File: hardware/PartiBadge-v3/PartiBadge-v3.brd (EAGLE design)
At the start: 118.9 x 117.7 mm, 26 parts, among them J1 I2C, J2 Supply, T1 MMBT4401-7-F

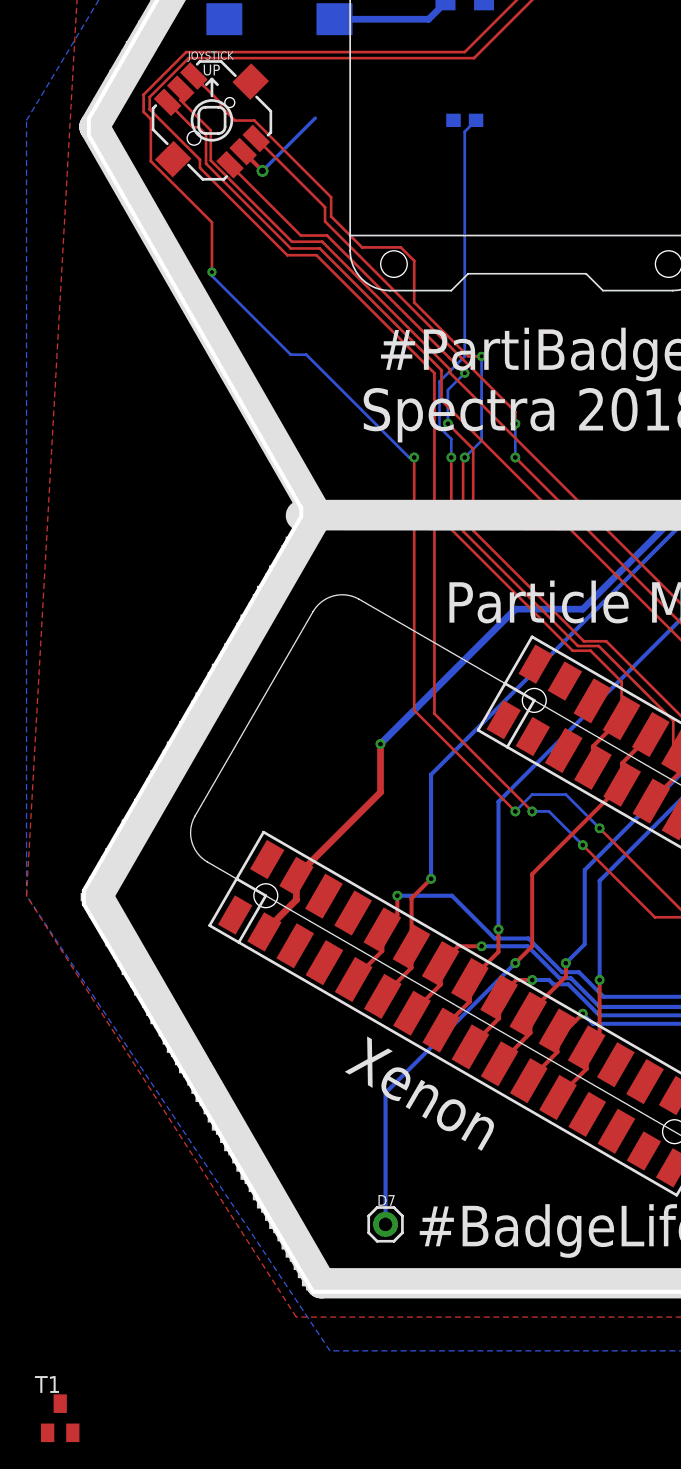
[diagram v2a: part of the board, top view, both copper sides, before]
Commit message: added transistor to layout
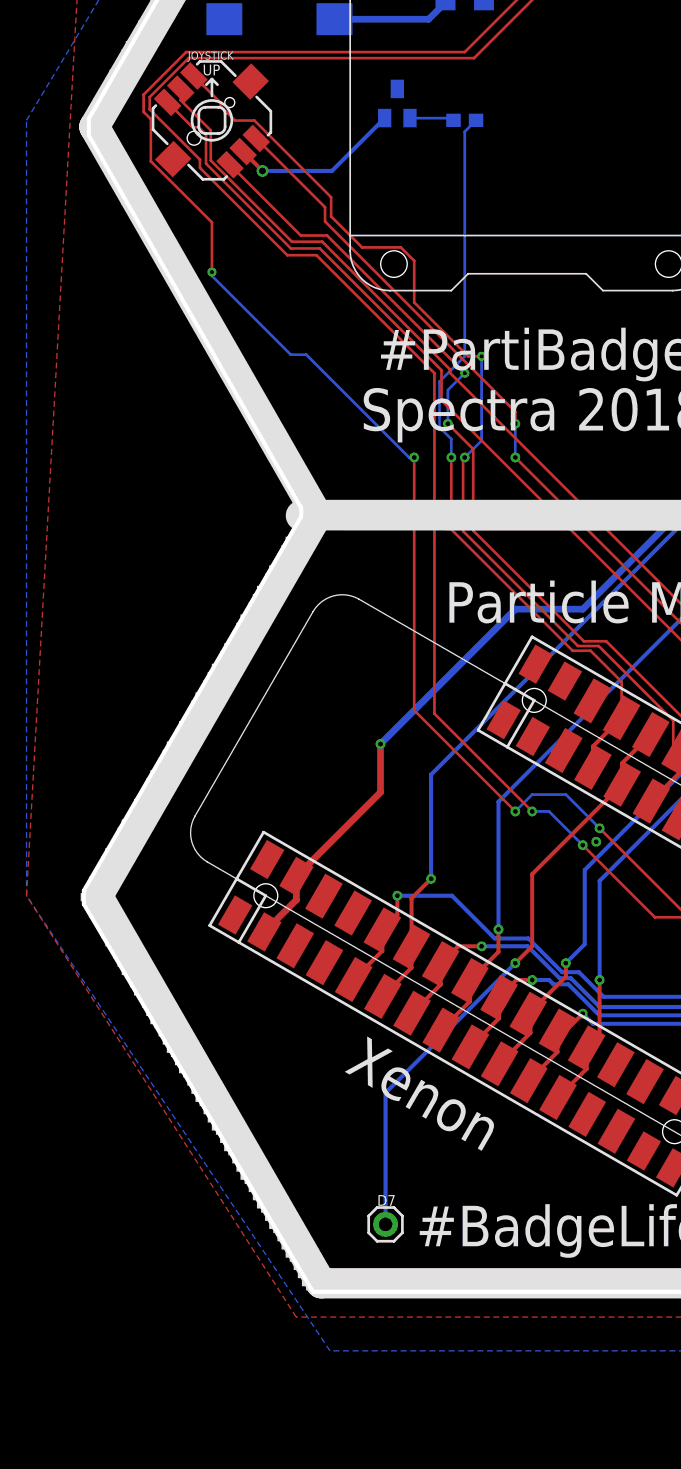
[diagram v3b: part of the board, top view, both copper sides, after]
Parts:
- moved T1 102.3 mm to (27.9, 92.7), flipped to the bottom
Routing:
- net GND: track 10.9 -> 16.2 mm
- net N$5: track 0.24 -> 3.59 mm
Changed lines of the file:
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@@
 <attribute name="PACKAGE" value=" PUI" x="19.05" y="99.06" size="1.778" layer="28" rot="MR0" display="off"/>
 </element>
-<element name="T1" library="transistor" library_urn="urn:adsk.eagle:library:402" package="SOT23-BEC" package3d_urn="urn:adsk.eagle:package:28748/2" value="MMBT4401-7-F" x="2.54" y="-6.35"/>
+<element name="T1" library="transistor" library_urn="urn:adsk.eagle:library:402" package="SOT23-BEC" package3d_urn="urn:adsk.eagle:package:28748/2" value="MMBT4401-7-F" x="27.94" y="92.71" rot="MR0"/>
 </elements>
 <signals>
@@
 <contactref element="D1" pad="A"/>
 <contactref element="LS1" pad="2"/>
-<wire x1="17.78" y1="87.63" x2="21.76" y2="91.61" width="0.254" layer="16"/>
 <contactref element="T1" pad="E"/>
 <contactref element="T1" pad="C"/>
-<wire x1="95.658" y1="77.383" x2="102.235" y2="83.693" width="0" layer="19" extent="1-1"/>
-<wire x1="89.408" y1="73.133" x2="95.658" y2="77.383" width="0" layer="19" extent="1-1"/>
-<wire x1="76.1" y1="59.73" x2="89.408" y2="73.133" width="0" layer="19" extent="1-1"/>
-<wire x1="69.85" y1="55.48" x2="76.1" y2="59.73" width="0" layer="19" extent="1-1"/>
-<wire x1="89.789" y1="38.97" x2="76.1" y2="59.73" width="0" layer="19" extent="1-1"/>
-<wire x1="96.039" y1="43.22" x2="89.789" y2="38.97" width="0" layer="19" extent="1-1"/>
-<wire x1="107.95" y1="55.48" x2="96.039" y2="43.22" width="0" layer="19" extent="1-1"/>
-<wire x1="114.2" y1="59.73" x2="107.95" y2="55.48" width="0" layer="19" extent="1-1"/>
-<wire x1="59.69" y1="99.06" x2="89.408" y2="73.133" width="0" layer="19" extent="1-1"/>
-<wire x1="57.15" y1="106.68" x2="59.69" y2="99.06" width="0" layer="19" extent="1-1"/>
-<wire x1="48.68" y1="107.95" x2="56.06" y2="106.68" width="0" layer="19" extent="1-16"/>
-<wire x1="36.724" y1="104.213" x2="46.736" y2="107.442" width="0" layer="19" extent="16-16"/>
-<wire x1="34.47" y1="100.33" x2="36.724" y2="104.213" width="0" layer="19" extent="16-16"/>
-<wire x1="21.76" y1="91.61" x2="34.47" y2="100.33" width="0" layer="19" extent="16-16"/>
-<wire x1="14.9" y1="99.06" x2="16.321128125" y2="89.08886875" width="0" layer="19" extent="1-16"/>
-<wire x1="24.607871875" y1="31.714746875" x2="69.85" y2="55.48" width="0" layer="19" extent="1-1"/>
-<wire x1="22.448871875" y1="27.97525" x2="24.607871875" y2="31.714746875" width="0" layer="19" extent="1-1"/>
-<wire x1="2.54" y1="-5.25" x2="22.448871875" y2="27.97525" width="0" layer="19" extent="1-1"/>
-<wire x1="3.49" y1="-7.45" x2="2.54" y2="-5.25" width="0" layer="19" extent="1-1"/>
+<wire x1="17.78" y1="87.63" x2="23.01" y2="87.63" width="0.3048" layer="16"/>
+<wire x1="23.01" y1="87.63" x2="26.99" y2="91.61" width="0.3048" layer="16"/>
 </signal>
 <signal name="+3V3">
@@
 <wire x1="32" y1="91.61" x2="32.17" y2="91.44" width="0.254" layer="16"/>
 <contactref element="T1" pad="B"/>
-<wire x1="1.59" y1="-7.45" x2="32.17" y2="91.44" width="0" layer="19" extent="1-16"/>
+<wire x1="28.89" y1="91.61" x2="32" y2="91.61" width="0.2032" layer="16"/>
+<wire x1="32" y1="91.61" x2="32.17" y2="91.44" width="0.2032" layer="16"/>
+</signal>
+<signal name="N$2">
+<via x="42.926" y="37.084" extent="1-16" drill="0.35"/>
 </signal>
 </signals>

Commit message: finished Xenon port
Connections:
- new net N$18: D1.A, T1.C
- net GND: no longer D1.A, T1.C
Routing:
- net N$18: track 0.00 -> 9.23 mm
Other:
- outline, holes or cut-outs redrawn
- board text added: "*NON PLATED * *SLOT*"
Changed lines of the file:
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@@
 <drawing>
 <settings>
-<setting alwaysvectorfont="no"/>
+<setting alwaysvectorfont="yes"/>
 <setting verticaltext="up"/>
 </settings>
-<grid distance="50" unitdist="mil" unit="mil" style="lines" multiple="1" display="no" altdistance="5" altunitdist="mil" altunit="mil"/>
+<grid distance="5" unitdist="mil" unit="mil" style="dots" multiple="1" display="yes" altdistance="5" altunitdist="mil" altunit="mil"/>
 <layers>
 <layer number="1" name="Top" color="4" fill="1" visible="yes" active="yes"/>
@@
 <layer number="26" name="bNames" color="7" fill="1" visible="yes" active="yes"/>
 <layer number="27" name="tValues" color="7" fill="1" visible="yes" active="yes"/>
-<layer number="28" name="bValues" color="7" fill="1" visible="yes" active="yes"/>
+<layer number="28" name="bValues" color="7" fill="1" visible="no" active="yes"/>
 <layer number="29" name="tStop" color="7" fill="3" visible="no" active="yes"/>
 <layer number="30" name="bStop" color="7" fill="6" visible="no" active="yes"/>
@@
 <layer number="45" name="Holes" color="7" fill="1" visible="yes" active="yes"/>
 <layer number="46" name="Milling" color="3" fill="1" visible="no" active="yes"/>
-<layer number="47" name="Measures" color="7" fill="1" visible="no" active="yes"/>
+<layer number="47" name="Measures" color="7" fill="1" visible="yes" active="yes"/>
 <layer number="48" name="Document" color="7" fill="1" visible="yes" active="yes"/>
 <layer number="49" name="Reference" color="7" fill="1" visible="yes" active="yes"/>
@@
 <wire x1="4.318" y1="33.401" x2="20.701" y2="61.595" width="0.3048" layer="20"/>
 <wire x1="20.701" y1="61.595" x2="20.701" y2="62.23" width="0.3048" layer="20"/>
-<text x="26.416" y="72.644" size="3.048" layer="21" font="vector" ratio="18">#PartiBadge</text>
-<text x="25.146" y="68.072" size="3.1496" layer="21" font="vector" ratio="18">Spectra 2018</text>
-<circle x="38.1" y="114.3" radius="4.57905" width="0.4064" layer="20"/>
+<text x="26.67" y="72.644" size="3.048" layer="21" font="vector" ratio="18">#PartiBadge</text>
+<text x="25.4" y="67.691" size="3.1496" layer="21" font="vector" ratio="18">Spectra 2018</text>
+<circle x="38.1" y="114.3" radius="4.318" width="0.4064" layer="20"/>
 <text x="65.024" y="68.58" size="2.4384" layer="21" font="vector" ratio="18">A</text>
 <text x="84.455" y="86.233" size="2.4384" layer="21" font="vector" ratio="18">B</text>
@@
 <rectangle x1="119.3546" y1="103.5812" x2="157.4546" y2="106.1212" layer="49"/>
 <rectangle x1="119.3546" y1="98.5012" x2="157.4546" y2="101.0412" layer="49"/>
-<dimension x1="2.54" y1="57.15" x2="104.14" y2="57.15" x3="53.34" y3="132.334" textsize="1.778" layer="47" dtype="diameter" unit="inch" visible="yes"/>
-<dimension x1="48.76095" y1="101.6" x2="57.91905" y2="101.6" x3="53.34" y3="124.46" textsize="1.778" layer="47" dtype="diameter" unit="inch" visible="yes"/>
 <dimension x1="51.689" y1="83.058" x2="64.008" y2="83.058" x3="57.8485" y3="111.125" textsize="1.778" layer="47" visible="yes"/>
-<dimension x1="61.71543125" y1="83.057990625" x2="61.72856875" y2="78.486009375" x3="105.918" y3="80.898996875" textsize="1.778" layer="47" dtype="diameter" visible="yes"/>
 <text x="23.876" y="19.812" size="3.1496" layer="21" font="vector" ratio="18" rot="R330">Xenon</text>
 <text x="31.496" y="53.594" size="3.048" layer="21" font="vector" ratio="18">Particle Mesh</text>
+<wire x1="47.625" y1="30.861" x2="55.499" y2="30.861" width="0.1524" layer="20"/>
+<wire x1="47.752" y1="26.416" x2="55.372" y2="26.416" width="0.1524" layer="20"/>
+<wire x1="55.499" y1="30.861" x2="55.626" y2="30.861" width="0.1524" layer="20"/>
+<wire x1="47.625" y1="30.861" x2="55.626" y2="30.861" width="0.1524" layer="20"/>
+<wire x1="55.626" y1="30.861" x2="55.626" y2="26.416" width="0.1524" layer="20" curve="-180"/>
+<wire x1="55.626" y1="26.416" x2="47.625" y2="26.416" width="0.1524" layer="20"/>
+<wire x1="47.625" y1="26.416" x2="47.625" y2="30.861" width="0.1524" layer="20" curve="-180"/>
+<text x="87.63" y="5.08" size="1.778" layer="48">*NON PLATED *
+*SLOT*</text>
+<wire x1="86.36" y1="7.62" x2="58.42" y2="25.4" width="0.1524" layer="48"/>
+<wire x1="58.42" y1="25.4" x2="59.69" y2="22.86" width="0.1524" layer="48"/>
+<wire x1="59.69" y1="22.86" x2="60.96" y2="25.4" width="0.1524" layer="48"/>
+<wire x1="60.96" y1="25.4" x2="58.42" y2="25.4" width="0.1524" layer="48"/>
+<dimension x1="47.625" y1="30.861" x2="47.625" y2="26.416" x3="115.951" y3="28.6385" textsize="1.778" layer="47" dtype="vertical"/>
 </plain>
 <attributes>
@@
 </polygon>
 <polygon width="0.3048" layer="1" isolate="0.3048">
-<vertex x="5.08" y="123.19"/>
+<vertex x="4.34483125" y="123.19"/>
 <vertex x="82.55" y="123.19"/>
 <vertex x="125.73" y="80.01"/>
@@
 <vertex x="55.88" y="1.27"/>
 <vertex x="20.32" y="1.27"/>
-<vertex x="0" y="33.02"/>
+<vertex x="-0.675690625" y="34.075765625"/>
 </polygon>
 <wire x1="16.321128125" y1="89.08886875" x2="17.779996875" y2="87.63" width="0.3048" layer="1"/>
@@
 <contactref element="MS1" pad="4'"/>
 <contactref element="MS1" pad="4"/>
-<contactref element="D1" pad="A"/>
 <contactref element="LS1" pad="2"/>
 <contactref element="T1" pad="E"/>
-<contactref element="T1" pad="C"/>
 <wire x1="17.78" y1="87.63" x2="23.01" y2="87.63" width="0.3048" layer="16"/>
 <wire x1="23.01" y1="87.63" x2="26.99" y2="91.61" width="0.3048" layer="16"/>
@@
 </signal>
 <signal name="N$2">
-<via x="42.926" y="37.084" extent="1-16" drill="0.35"/>
+<via x="35.56" y="67.31" extent="1-16" drill="0.35"/>
+</signal>
+<signal name="N$6">
+<via x="34.544" y="65.913" extent="1-16" drill="0.35"/>
+</signal>
+<signal name="N$9">
+<via x="45.339" y="51.689" extent="1-16" drill="0.35"/>
+</signal>
+<signal name="N$11">
+<via x="46.99" y="49.911" extent="1-16" drill="0.35"/>
+</signal>
+<signal name="N$12">
+<via x="55.118" y="43.688" extent="1-16" drill="0.35"/>
+</signal>
+<signal name="N$13">
+<via x="57.277" y="42.291" extent="1-16" drill="0.35"/>
+</signal>
+<signal name="N$14">
+<via x="45.339" y="34.544" extent="1-16" drill="0.35"/>
+</signal>
+<signal name="N$15">
+<via x="46.609" y="35.941" extent="1-16" drill="0.35"/>
+</signal>
+<signal name="N$16">
+<via x="39.37" y="30.48" extent="1-16" drill="0.35"/>
+</signal>
+<signal name="N$17">
+<via x="36.83" y="31.75" extent="1-16" drill="0.35"/>
+</signal>
+<signal name="N$18">
+<contactref element="D1" pad="A"/>
+<contactref element="T1" pad="C"/>
+<wire x1="27.94" y1="93.81" x2="34.46" y2="100.33" width="0.3048" layer="16"/>
+<wire x1="34.46" y1="100.33" x2="34.47" y2="100.33" width="0.3048" layer="16"/>
+</signal>
+<signal name="N$19">
+<via x="40.64" y="39.37" extent="1-16" drill="0.35"/>
 </signal>
 </signals>
@@
 </drawing>
 <compatibility>
+<note version="6.3" minversion="6.2.2" severity="warning">
+Since Version 6.2.2 text objects can contain more than one line,
+which will not be processed correctly with this version.
+</note>
 <note version="8.2" severity="warning">
 Since Version 8.2, EAGLE supports online libraries. The ids

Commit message: piezo tweak from Frank
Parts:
- added R7: 33R, SparkFun-Resistors:0603
- added U$1, U$2: SPARK_LOGO_WITH_PLANE, Spark:SPARK_LOGO_PLUS_PLANE
- moved D1 5.97 mm to (27.8, 97.4)
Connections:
- new net N$20: D1.C, LS1.1, R7.1
- net +3V3: now also R7.2; no longer D1.C, LS1.1
- net GND: no longer LS1.2
- net N$18: now also LS1.2
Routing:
- net N$18: track 9.23 -> 19.4 mm
- net +3V3: track 124.7 -> 115.9 mm
- net N$20: track 0.00 -> 7.46 mm
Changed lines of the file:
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@@
 <?xml version="1.0" encoding="utf-8"?>
 <!DOCTYPE eagle SYSTEM "eagle.dtd">
-<eagle version="9.1.3">
+<eagle version="9.1.1">
 <drawing>
 <settings>
-<setting alwaysvectorfont="yes"/>
+<setting alwaysvectorfont="no"/>
 <setting verticaltext="up"/>
 </settings>
@@
 </element>
 <element name="MS1" library="Particle-Mesh" package="FEATHERWING_SMT2" value="PARTICLE_MESH_SMTDUAL" x="11.43" y="36.83" rot="R330"/>
-<element name="D1" library="diode" library_urn="urn:adsk.eagle:library:210" package="SOD323-W" package3d_urn="urn:adsk.eagle:package:43418/1" value="" x="33.02" y="100.33" rot="MR180"/>
+<element name="D1" library="diode" library_urn="urn:adsk.eagle:library:210" package="SOD323-W" package3d_urn="urn:adsk.eagle:package:43418/1" value="" x="27.813" y="97.409" rot="MR180"/>
 <element name="R8" library="SparkFun-Resistors" library_urn="urn:adsk.eagle:library:532" package="0603" package3d_urn="urn:adsk.eagle:package:39650/1" value="1k" x="33.02" y="91.44" rot="MR180">
 <attribute name="PROD_ID" value="RES-00824" x="33.02" y="91.44" size="1.778" layer="28" rot="MR180" display="off"/>
@@
 </element>
 <element name="T1" library="transistor" library_urn="urn:adsk.eagle:library:402" package="SOT23-BEC" package3d_urn="urn:adsk.eagle:package:28748/2" value="MMBT4401-7-F" x="27.94" y="92.71" rot="MR0"/>
+<element name="R7" library="SparkFun-Resistors" library_urn="urn:adsk.eagle:library:532" package="0603" package3d_urn="urn:adsk.eagle:package:39650/1" value="33R" x="27.813" y="100.33" rot="MR180">
+<attribute name="PROD_ID" value="RES-00824" x="27.813" y="100.33" size="1.778" layer="28" rot="MR180" display="off"/>
+</element>
+<element name="U$1" library="Spark" package="SPARK_LOGO_PLUS_PLANE" value="SPARK_LOGO_WITH_PLANE" x="51.943" y="8.001"/>
+<element name="U$2" library="Spark" package="SPARK_LOGO_PLUS_PLANE" value="SPARK_LOGO_WITH_PLANE" x="51.943" y="8.001" rot="MR0"/>
 </elements>
 <signals>
@@
 <contactref element="MS1" pad="4'"/>
 <contactref element="MS1" pad="4"/>
-<contactref element="LS1" pad="2"/>
 <contactref element="T1" pad="E"/>
 <wire x1="17.78" y1="87.63" x2="23.01" y2="87.63" width="0.3048" layer="16"/>
@@
 <wire x1="58.4743375" y1="97.79" x2="62.23" y2="97.79" width="0.508" layer="1"/>
 <wire x1="100.5904" y1="87.8776" x2="102.235" y2="86.233" width="0.508" layer="16"/>
-<via x="72.39" y="86.36" extent="1-16" drill="0.5"/>
-<wire x1="72.39" y1="86.36" x2="73.9076" y2="87.8776" width="0.508" layer="16"/>
-<wire x1="73.9076" y1="87.8776" x2="100.5904" y2="87.8776" width="0.508" layer="16"/>
+<via x="74.168" y="87.884" extent="1-16" drill="0.5"/>
+<wire x1="74.1744" y1="87.8776" x2="74.168" y2="87.884" width="0.508" layer="16"/>
+<wire x1="74.1744" y1="87.8776" x2="100.5904" y2="87.8776" width="0.508" layer="16"/>
 <contactref element="R5" pad="2"/>
 <contactref element="R6" pad="2"/>
@@
 <wire x1="37.457425" y1="106.7784" x2="42.0084" y2="106.7784" width="0.508" layer="16"/>
 <wire x1="42.0084" y1="106.7784" x2="42.037" y2="106.807" width="0.508" layer="16"/>
-<wire x1="72.39" y1="87.63" x2="72.39" y2="86.36" width="0.508" layer="1"/>
-<wire x1="62.23" y1="97.79" x2="72.39" y2="87.63" width="0.508" layer="1"/>
+<wire x1="74.168" y1="87.884" x2="72.136" y2="87.884" width="0.508" layer="1"/>
+<wire x1="62.23" y1="97.79" x2="72.136" y2="87.884" width="0.508" layer="1"/>
 <contactref element="S5" pad="1"/>
 <wire x1="58.4743375" y1="97.79" x2="58.4743375" y2="97.79" width="0.508" layer="1"/>
 <wire x1="57.15" y1="91.44" x2="57.15" y2="99.06" width="0.508" layer="1"/>
 <wire x1="57.15" y1="99.06" x2="57.17716875" y2="99.08716875" width="0.508" layer="1"/>
-<contactref element="D1" pad="C"/>
-<contactref element="LS1" pad="1"/>
-<wire x1="23.2" y1="99.06" x2="30.3" y2="99.06" width="0.508" layer="16"/>
-<wire x1="30.3" y1="99.06" x2="31.57" y2="100.33" width="0.508" layer="16"/>
-<wire x1="31.57" y1="100.33" x2="34.184" y2="102.944" width="0.508" layer="16"/>
-<wire x1="34.184" y1="102.944" x2="34.184" y2="104.213" width="0.508" layer="16"/>
+<contactref element="R7" pad="2"/>
+<wire x1="28.663" y1="100.33" x2="32.546" y2="104.213" width="0.508" layer="16"/>
+<wire x1="32.546" y1="104.213" x2="34.184" y2="104.213" width="0.508" layer="16"/>
 </signal>
 <signal name="N$4">
@@
 <contactref element="MS1" pad="18" route="any" routetag="G$1.SCL"/>
 <contactref element="MS1" pad="18'" route="any" routetag="G$1.SCL"/>
-<wire x1="60.361621875" y1="37.762059375" x2="60.361621875" y2="36.847846875" width="0.3048" layer="1"/>
-<wire x1="60.361621875" y1="36.847846875" x2="59.05016875" y2="35.53639375" width="0.3048" layer="1"/>
-<wire x1="59.05016875" y1="35.53639375" x2="59.05016875" y2="34.684165625" width="0.3048" layer="1"/>
-<wire x1="59.05016875" y1="34.684165625" x2="57.948621875" y2="33.58261875" width="0.3048" layer="1"/>
 <wire x1="57.948621875" y1="33.58261875" x2="57.71261875" y2="33.58261875" width="0.2032" layer="1"/>
 <wire x1="57.71261875" y1="33.58261875" x2="55.88" y2="31.75" width="0.2032" layer="1"/>
@@
 <wire x1="25.2095" y1="69.6595" x2="28.829" y2="66.04" width="0.2032" layer="16"/>
 <wire x1="28.829" y1="66.04" x2="29.21" y2="66.04" width="0.2032" layer="16"/>
+<wire x1="57.948621875" y1="33.58261875" x2="57.948621875" y2="35.349059375" width="0.3048" layer="1"/>
+<wire x1="57.948621875" y1="35.349059375" x2="60.361621875" y2="37.762059375" width="0.3048" layer="1"/>
 </signal>
 <signal name="UP">
@@
 <via x="36.83" y="31.75" extent="1-16" drill="0.35"/>
 </signal>
+<signal name="N$19">
+<via x="40.64" y="39.37" extent="1-16" drill="0.35"/>
+</signal>
 <signal name="N$18">
+<contactref element="LS1" pad="2"/>
 <contactref element="D1" pad="A"/>
 <contactref element="T1" pad="C"/>
-<wire x1="27.94" y1="93.81" x2="34.46" y2="100.33" width="0.3048" layer="16"/>
-<wire x1="34.46" y1="100.33" x2="34.47" y2="100.33" width="0.3048" layer="16"/>
-</signal>
-<signal name="N$19">
-<via x="40.64" y="39.37" extent="1-16" drill="0.35"/>
+<wire x1="29.253" y1="97.409" x2="29.263" y2="97.409" width="0.3048" layer="16"/>
+<wire x1="29.263" y1="97.409" x2="29.263" y2="95.133" width="0.3048" layer="16"/>
+<wire x1="29.263" y1="95.133" x2="27.94" y2="93.81" width="0.3048" layer="16"/>
+<wire x1="14.9" y1="99.06" x2="15.154" y2="98.806" width="0.508" layer="16"/>
+<wire x1="15.154" y1="98.806" x2="18.161" y2="98.806" width="0.508" layer="16"/>
+<wire x1="18.161" y1="98.806" x2="23.157" y2="93.81" width="0.508" layer="16"/>
+<wire x1="23.157" y1="93.81" x2="27.94" y2="93.81" width="0.508" layer="16"/>
+</signal>
+<signal name="N$20">
+<contactref element="D1" pad="C"/>
+<contactref element="LS1" pad="1"/>
+<contactref element="R7" pad="1"/>
+<wire x1="26.363" y1="97.409" x2="26.363" y2="99.73" width="0.3048" layer="16"/>
+<wire x1="26.363" y1="99.73" x2="26.963" y2="100.33" width="0.3048" layer="16"/>
+<wire x1="23.2" y1="99.06" x2="24.47" y2="100.33" width="0.508" layer="16"/>
+<wire x1="24.47" y1="100.33" x2="26.963" y2="100.33" width="0.508" layer="16"/>
 </signal>
 </signals>

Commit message: finalized v3 design
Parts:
- added U$6: (no value), particle-spark:SPARK-LOGO
- moved U$4 52.6 mm to (38.0, 76.6)
- moved YELLOW 3.67 mm to (88.9, 42.2)
- moved BLUE 1.61 mm to (88.9, 81.4)
- moved GREEN 0.38 mm to (108.0, 61.8)
- moved D7 0.28 mm to (27.3, 8.13)
- moved RED 0.25 mm to (69.8, 62.0)
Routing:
- net N$10: track 5.10 -> 8.29 mm
- net BUTTON_Y: track 77.6 -> 75.3 mm
- net +3V3: track 115.9 -> 117.4 mm
- net BUTTON_G: track 99.6 -> 100.8 mm
- net BUTTON_B: track 93.6 -> 94.2 mm
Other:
- outline, holes or cut-outs redrawn
- board text removed: "Particle.io"
